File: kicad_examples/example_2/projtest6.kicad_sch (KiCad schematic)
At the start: 6 parts

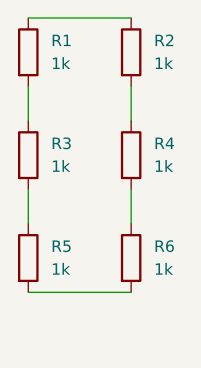
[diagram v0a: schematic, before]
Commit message: update
This commit adds a new KiCad project file with various design settings, rules, and configurations for a PCB layout.
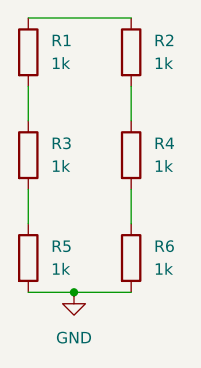
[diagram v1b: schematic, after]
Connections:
- net GND: now reaches R5.2, R6.2
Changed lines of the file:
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@@
 	(generator_version "10.0")
 	(paper "A4")
+	(junction
+		(at 82.55 110.49)
+		(diameter 0)
+		(color 0 0 0 0)
+	)
 	(wire
 		(pts
@@
 	(wire
 		(pts
-			(xy 77.47 110.49) (xy 88.9 110.49)
+			(xy 77.47 110.49) (xy 82.55 110.49)
+		)
+		(stroke
+			(width 0)
+			(type default)
+		)
+	)
+	(wire
+		(pts
+			(xy 82.55 110.49) (xy 88.9 110.49)
 		)
 		(stroke
@@
 					(unit 1)
 				)
+			)
+		)
+	)
+	(symbol
+		(lib_id "power:GND")
+		(at 82.55 110.49 0)
+		(unit 1)
+		(body_style 1)
+		(exclude_from_sim no)
+		(in_bom yes)
+		(on_board yes)
+		(in_pos_files yes)
+		(dnp no)
+		(fields_autoplaced yes)
+		(property "Reference" "#PWR01"
+			(at 82.55 116.84 0)
+			(hide yes)
+			(show_name no)
+			(do_not_autoplace no)
+			(effects
+				(font
+					(size 1.27 1.27)
+				)
+			)
+		)
+		(property "Value" "GND"
+			(at 82.55 115.57 0)
+			(show_name no)
+			(do_not_autoplace no)
+			(effects
+				(font
+					(size 1.27 1.27)
+				)
+			)
+		)
+		(property "Footprint" ""
+			(at 82.55 110.49 0)
+			(hide yes)
+			(show_name no)
+			(do_not_autoplace no)
+			(effects
+				(font
+					(size 1.27 1.27)
+				)
+			)
+		)
+		(property "Datasheet" ""
+			(at 82.55 110.49 0)
+			(hide yes)
+			(show_name no)
+			(do_not_autoplace no)
+			(effects
+				(font
+					(size 1.27 1.27)
+				)
+			)
+		)
+		(property "Description" "Power symbol creates a global label with name \"GND\" , ground"
+			(at 82.55 110.49 0)
+			(hide yes)
+			(show_name no)
+			(do_not_autoplace no)
+			(effects
+				(font
+					(size 1.27 1.27)
+				)
+			)
+		)
+		(pin "1"
+		)
+		(instances
+			(project "projtest6"
+				(path "/e87491f1-4771-4981-898a-30d27cb9c54c"
+					(reference "#PWR01")
+					(unit 1)
+				)
